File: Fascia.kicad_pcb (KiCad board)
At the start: 6 copper layers, 148.2 x 163.5 mm, 118 parts, among them J1 Verdin iMX95, J10 RTC coin cell, J2 Power in, J3 CAN to ECU, J4 Panel LVDS (provisional), J5 Pre-outs to amp, J6 Mic, J7 USB-C CarPlay, J8 JTAG debug, J9 Buttons, Q1 NFET diode, Q2 NFET pass, Q3 NFET i2c xlat, Q4 NFET i2c xlat, U1 LM74930-Q1, U10 TPS2557-Q1, U2 LM61460-Q1, U3 TLV767-Q1, U4 TCAN1044V-Q1, U5 SN65DSI85-Q1, U6 TLV767-Q1 3V3, U7 SN74AXC4T245-Q1, U8 SN74AXC4T245-Q1, U9 PCM3168A-Q1

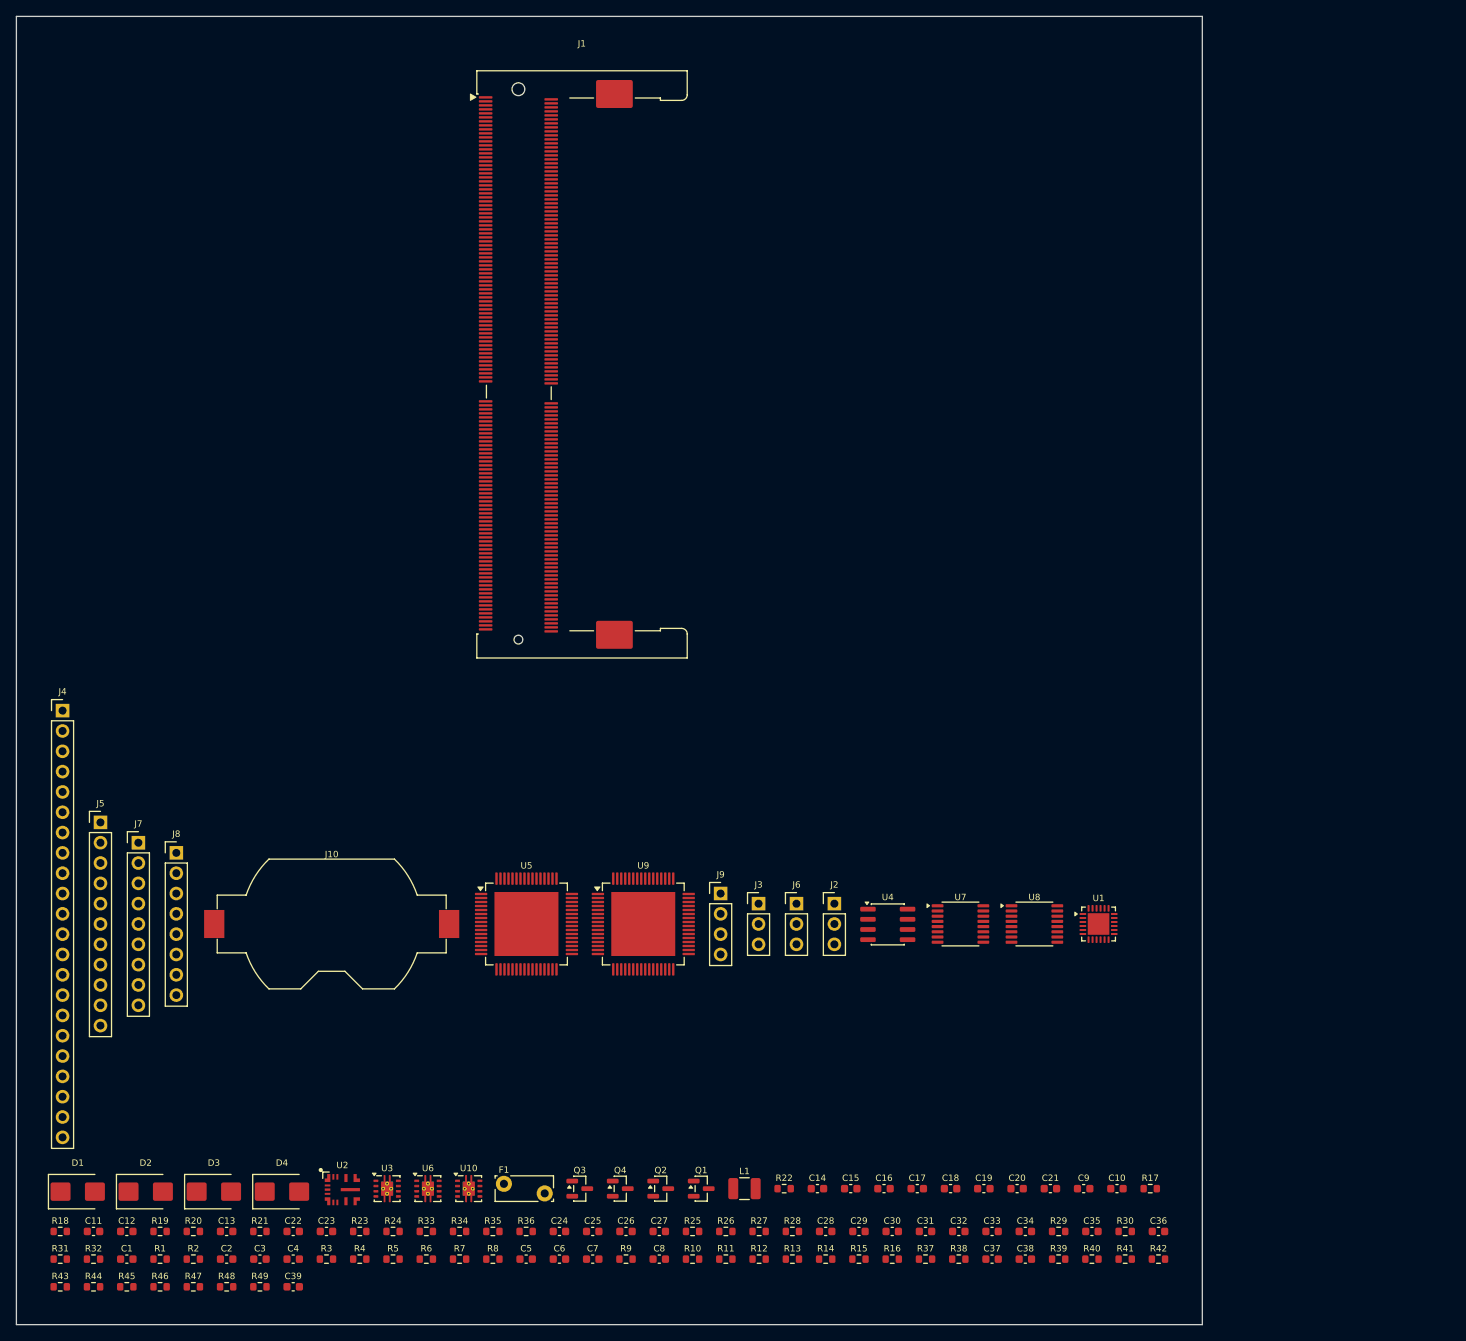
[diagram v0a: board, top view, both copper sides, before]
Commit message: Rotate the socket and group parts functionally: 164mm tall -> 92mm
Two changes, both prompted by the board looking like a parts bin.

The Verdin socket is now rotated 90 degrees. Its footprint is 36 x 79 mm,
tall and narrow, which forced a tall board and wasted the space beside
it. On its side it is 79 x 36 mm, the board becomes landscape - which is
also the shape a dash opening wants - and the height drops from 164 mm to
92 mm.

Parts are now grouped by connectivity rather than by size. Each
decoupling cap, divider and gate resistor is assigned to whichever IC or
connector it shares the most non-rail nets with, so every group is a real
functional block. Excluding rails from that count is what makes it work -
GND touches everything and would make every part look equally related to
everything else. The grouping comes from the netlist, so it cannot go
stale when the schematic changes.

Groups are placed with a skyline packer seeded with the socket as an
already-occupied region. Shelf packing wastes whatever vertical space the
tallest block in a row does not use, which on blocks this unequal is most
of it; and encoding the socket as a real packer input rather than a
collision check afterwards is the only arrangement that actually works.

Three real bugs found, each caught by a different mechanism:

- Rotating the socket produced 820 DRC violations, all J1 against
  ITSELF. The known gotcha is that a rotated footprint's pad shapes do
  not follow the parent angle, so each pad's angle must be set. What this
  board added: the angle must be ADDED to whatever the pad already had,
  not assigned. Every pad in the SODIMM-260 footprint already carries
  270 degrees - the edge fingers are oriented - and overwriting that with
  90 turned 0.3 x 1.7 mm pads at 0.5 mm pitch sideways into each other.

- footprint_bbox missed fp_arc MID points. An arc that bulges outward has
  its extreme at the mid point, so parts with curved outlines were
  understated - the coin-cell holder overl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
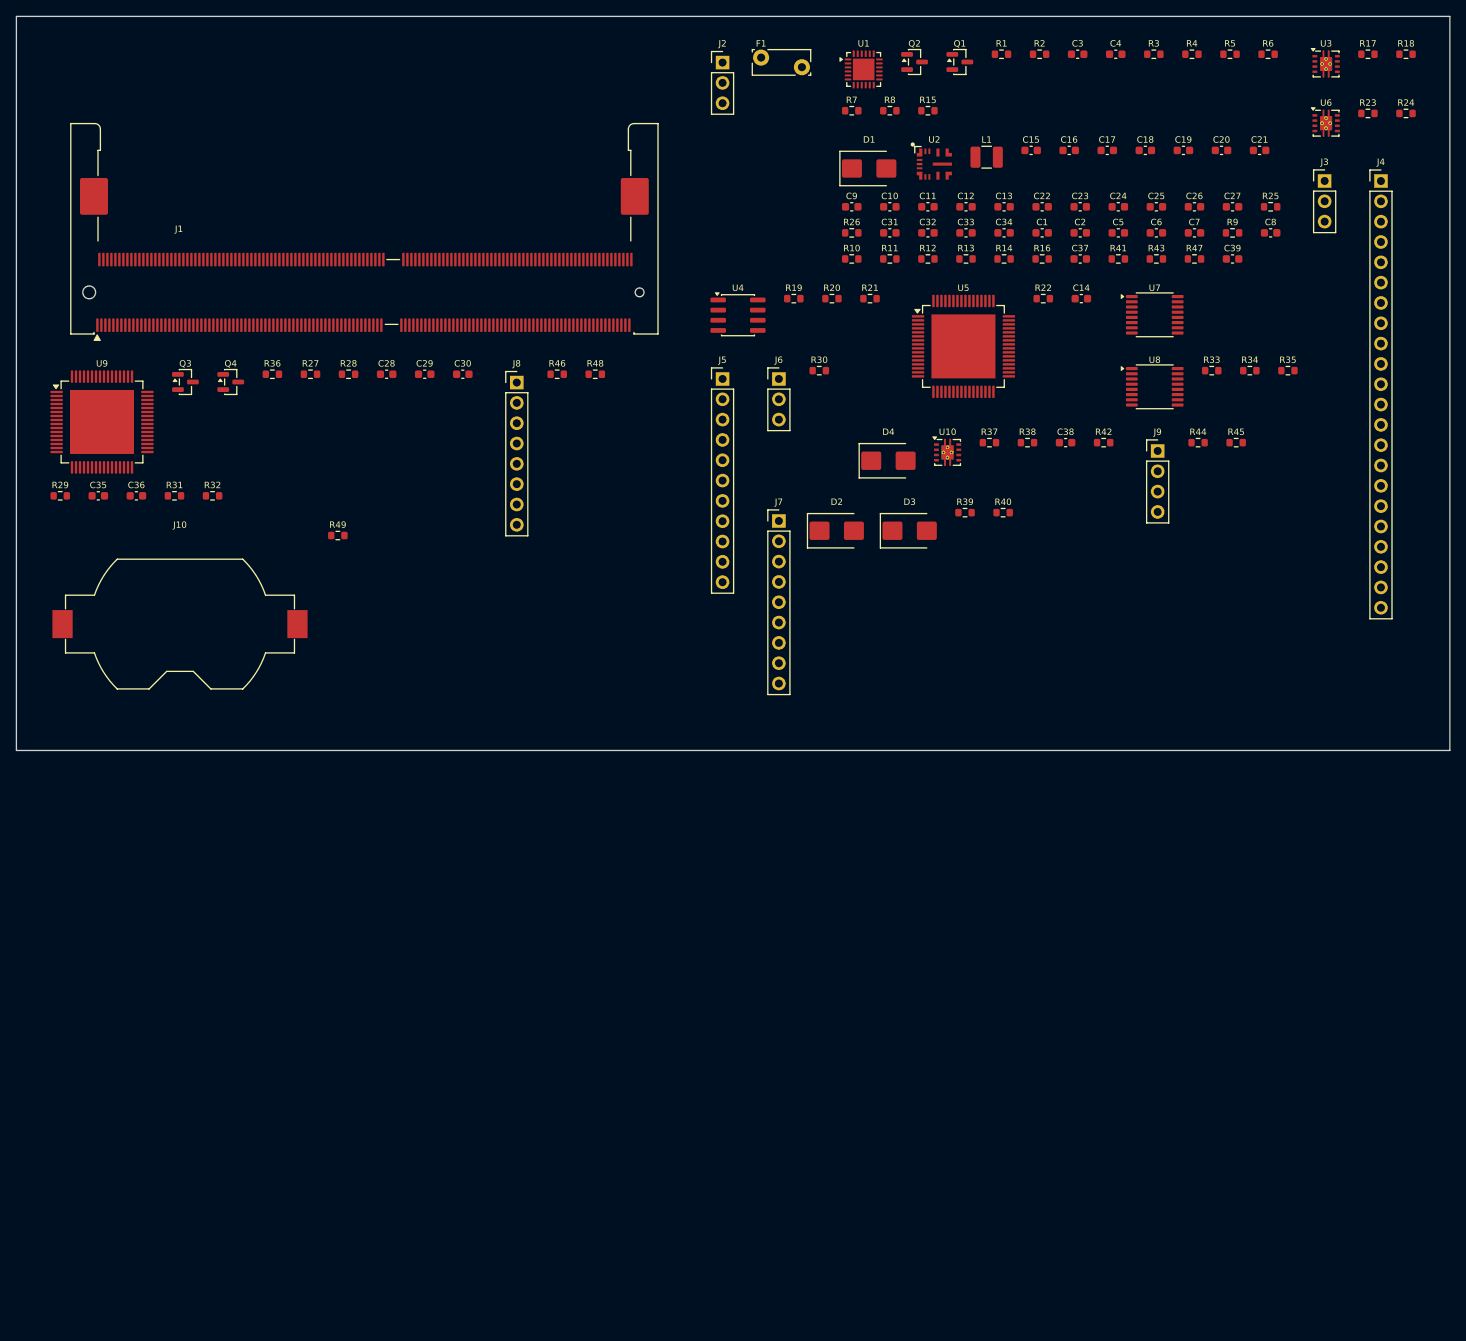
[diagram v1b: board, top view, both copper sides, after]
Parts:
- moved R18 223.5 mm to (173.7, 4.73)
- moved R24 188.6 mm to (173.7, 12.1)
- moved R23 188.2 mm to (168.9, 12.1)
- moved R43 187.8 mm to (142.5, 30.3)
- moved R2 184.0 mm to (127.9, 4.73)
- moved R6 183.7 mm to (156.5, 4.73)
- moved R1 183.7 mm to (123.1, 4.73)
- moved R5 183.4 mm to (151.7, 4.73)
- moved U3 183.1 mm to (163.7, 5.95)
- moved R4 183.0 mm to (146.9, 4.73)
- moved R3 182.7 mm to (142.2, 4.73)
- moved C4 182.4 mm to (137.4, 4.73)
- moved C3 182.0 mm to (132.7, 4.73)
- moved R47 179.4 mm to (147.3, 30.3)
- moved J4 177.6 mm to (170.6, 20.6)
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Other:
- board size 148.2 x 163.5 mm -> 179.2 x 91.8 mm

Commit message: Port the sibling skyline packer: board 179x92 -> 148x64
You were right that I had forgotten how we placed the other boards. This
replaces my shelf packer with the skyline bottom-left packer manifold-pcb
and thermo-pcb already use, ported rather than reinvented.

Two properties of that packer do the work, and my version had neither:

- Every part is tried BOTH unrotated and rotated 90 degrees, and goes
  wherever it yields the lowest top edge. That is what turns the tall
  pin-header connectors on their sides - 16 parts end up rotated - and
  lets the 0603s backfill the low spots beside big parts instead of being
  confined to a same-size block.
- Candidate positions include right-justifying against a segment's right
  edge, not just its left, which catches placements where snugging up
  against a taller neighbour fits better.

Kept the functional grouping from the previous pass as the sort order, so
each IC still keeps its own passives nearby, but large parts now go first
regardless of group. Pure group order had buried the coin-cell holder at
the end, where it landed in an empty row of its own and set the board
height; pure area order scatters each IC's passives away from it. The
split gets the awkward parts placed while the skyline is free and keeps
the small stuff with its IC.

Board is now 148.2 x 64.3 mm, down from 179 x 92 this morning and from
148 x 164 before the socket was rotated - a 61% area reduction overall.
DRC: schematic parity 0, and 3 cosmetic silkscreen clearances.

One thing tried and rejected: a reference-label lane assignment, trying
above then below then further out, checked against neighbours. It
measured WORSE - 14 silkscreen findings against 4 - because re-centring
every label disturbed the many that were already fine in order to rescue
the few that were not. Reverted, with the reason recorded at the call
site so it is not attempted again blind.

Also rejected: shrinking passive designators to 0.6 mm to buy clearance.
The board's own rules s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
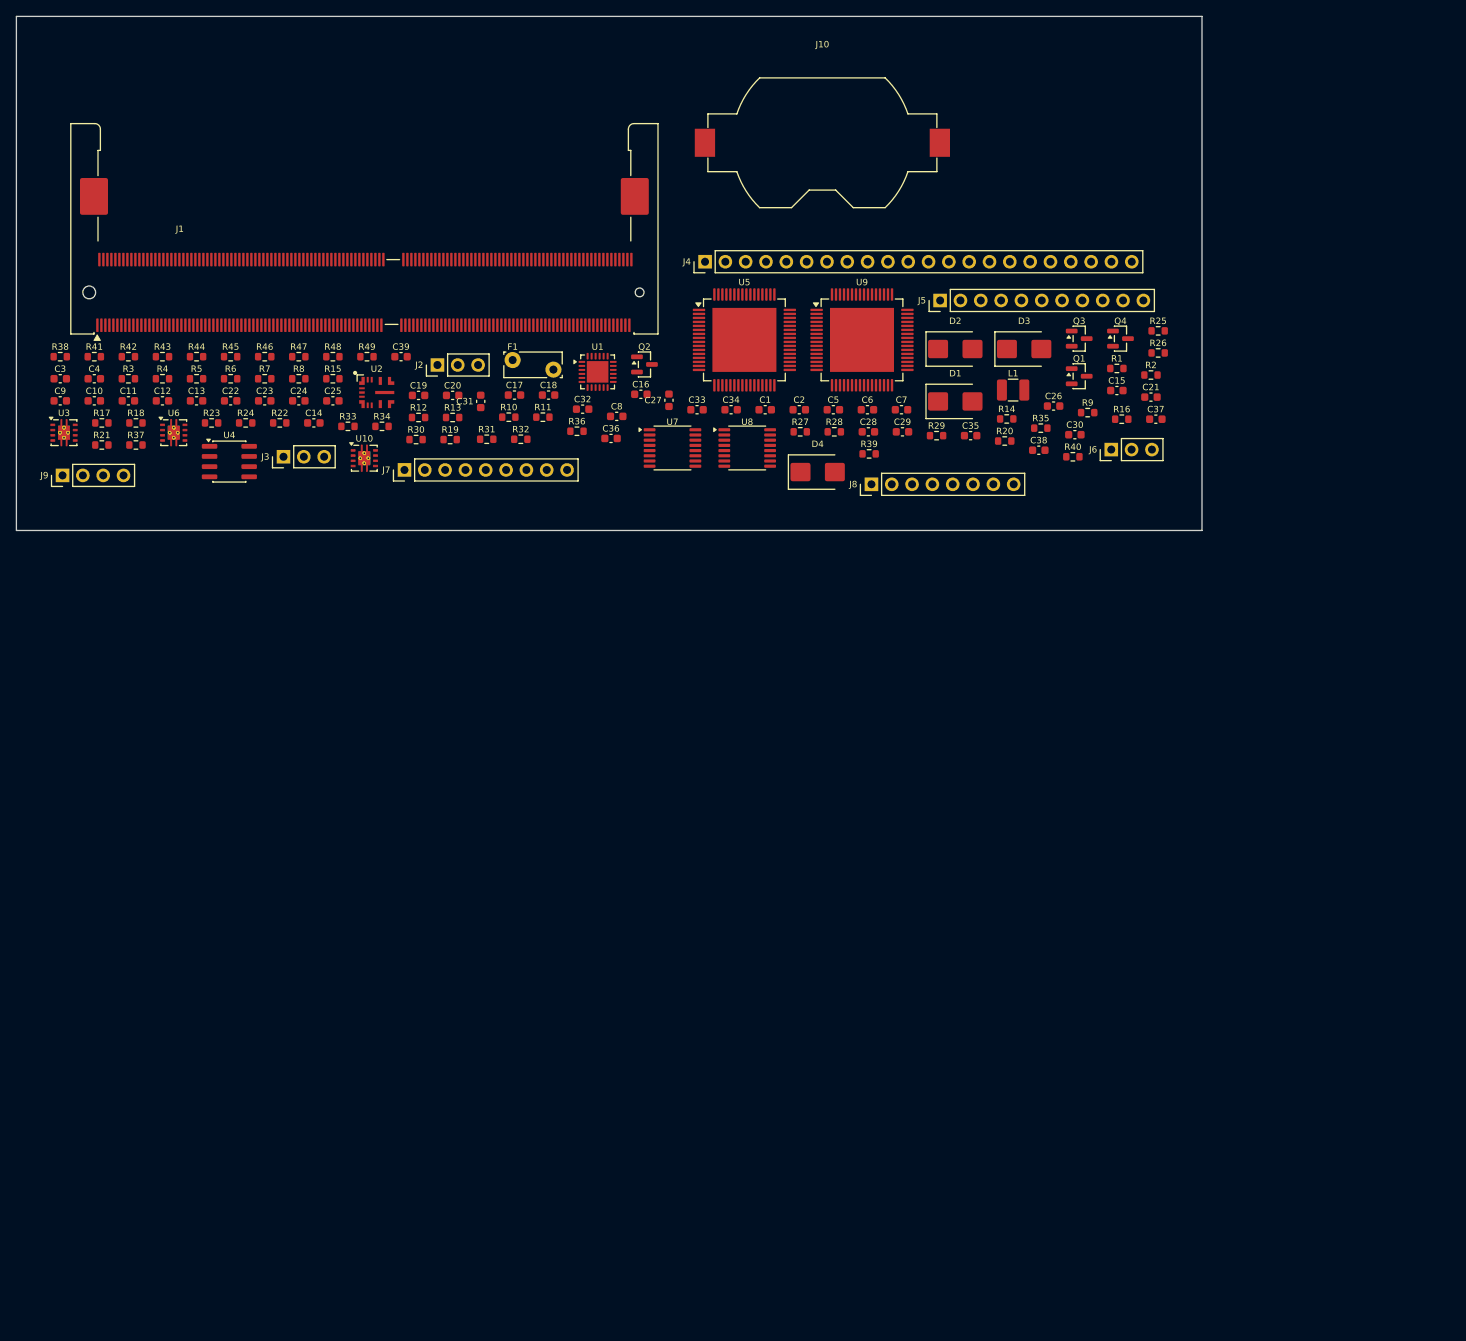
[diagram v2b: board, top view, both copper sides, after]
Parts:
- moved R18 165.3 mm to (14.9, 50.8)
- moved R17 164.8 mm to (10.7, 50.8)
- moved U3 164.4 mm to (5.95, 52.0)
- moved R24 150.1 mm to (28.7, 50.8)
- moved R23 149.6 mm to (24.4, 50.8)
- moved U6 149.1 mm to (19.7, 52.0)
- moved J9 136.9 mm to (5.77, 57.4), turned to 90 degrees
- moved R6 135.9 mm to (26.8, 45.3)
- moved R5 135.4 mm to (22.5, 45.3)
- moved R4 134.9 mm to (18.3, 45.3)
- moved J3 134.6 mm to (33.4, 55.0), turned to 90 degrees
- moved R3 134.4 mm to (14.0, 45.3)
- moved C4 134.0 mm to (9.74, 45.3)
- moved C3 133.5 mm to (5.48, 45.3)
- moved R41 128.6 mm to (9.74, 42.5)
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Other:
- board size 179.2 x 91.8 mm -> 148.2 x 64.3 mm
